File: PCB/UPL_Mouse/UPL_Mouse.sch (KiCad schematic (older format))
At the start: 10 parts, among them J1 PS2_5749180-1, J2 DB9_Female, J3 USB Micro_10118193-0001LF, J4 AVR-ISP-6, U1 MAX232DR, U2 ATTINY85-20SH

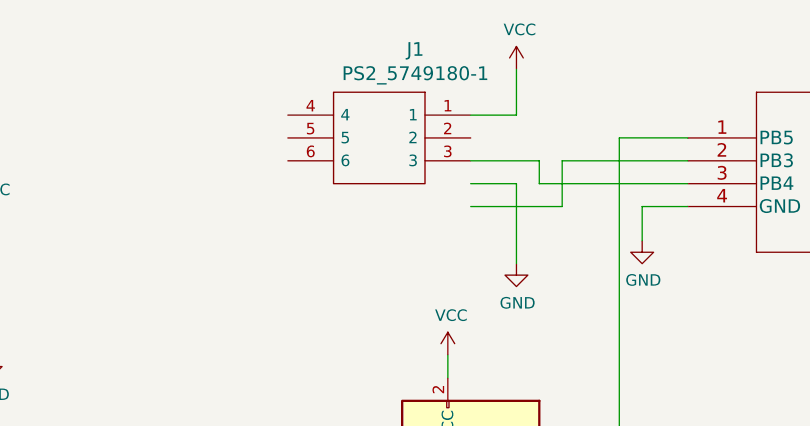
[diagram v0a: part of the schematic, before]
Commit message: Update Design and Code
Update in code regarding configuration of the chip.

Update in PCB due to wrong footprint mini din connector.
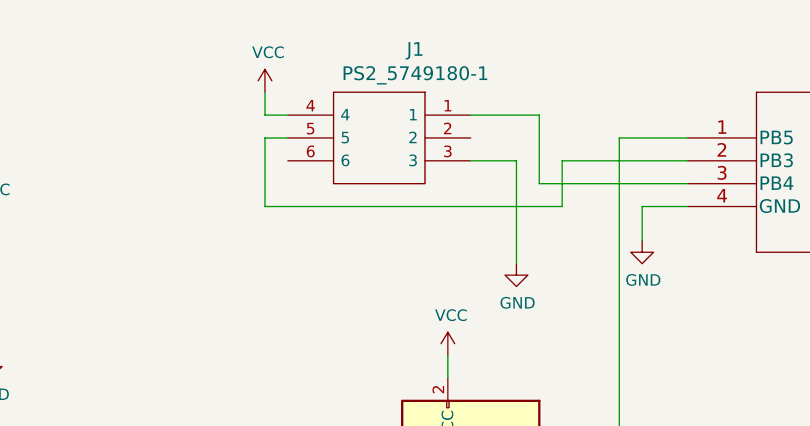
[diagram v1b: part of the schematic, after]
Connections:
- net GND: now also J1.3
- net VCC: now also J1.4; no longer J1.1
- net at U2.3 (PB4): now also J1.1; no longer J1.3
- net at J1.5: now also U2.2 (PB3)
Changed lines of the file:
@@
 	5250 2350 4600 2350
 Wire Wire Line
-	4600 2350 4600 2250
-Wire Wire Line
-	4600 2250 4300 2250
-Wire Wire Line
 	5250 2250 4700 2250
-Wire Wire Line
-	4700 2250 4700 2450
-Wire Wire Line
-	4700 2450 4300 2450
 Wire Wire Line
 	5050 2600 5050 2450
@@
 L power:VCC #PWR?
 U 1 1 6063A42F
-P 4500 1850
-F 0 "#PWR?" H 4500 1700 50  0001 C CNN
-F 1 "VCC" H 4515 2023 50  0000 C CNN
-F 2 "" H 4500 1850 50  0001 C CNN
-F 3 "" H 4500 1850 50  0001 C CNN
-	1    4500 1850
+P 3400 1950
+F 0 "#PWR?" H 3400 1800 50  0001 C CNN
+F 1 "VCC" H 3415 2123 50  0000 C CNN
+F 2 "" H 3400 1950 50  0001 C CNN
+F 3 "" H 3400 1950 50  0001 C CNN
+	1    3400 1950
 	1    0    0    -1
 $EndComp
-Wire Wire Line
-	4300 2350 4500 2350
-Wire Wire Line
-	4500 2350 4500 2700
-Wire Wire Line
-	4300 2050 4500 2050
-Wire Wire Line
-	4500 2050 4500 1850
 $Comp
 L power:VCC #PWR?
@@
 Wire Wire Line
 	2200 3050 2200 3100
+Wire Wire Line
+	3500 2050 3400 2050
+Wire Wire Line
+	3400 2050 3400 1950
+Wire Wire Line
+	4300 2250 4500 2250
+Wire Wire Line
+	4500 2250 4500 2700
+Wire Wire Line
+	3500 2150 3400 2150
+Wire Wire Line
+	3400 2150 3400 2450
+Wire Wire Line
+	3400 2450 4700 2450
+Wire Wire Line
+	4700 2450 4700 2250
+Wire Wire Line
+	4300 2050 4600 2050
+Wire Wire Line
+	4600 2050 4600 2350
 $EndSCHEMATC

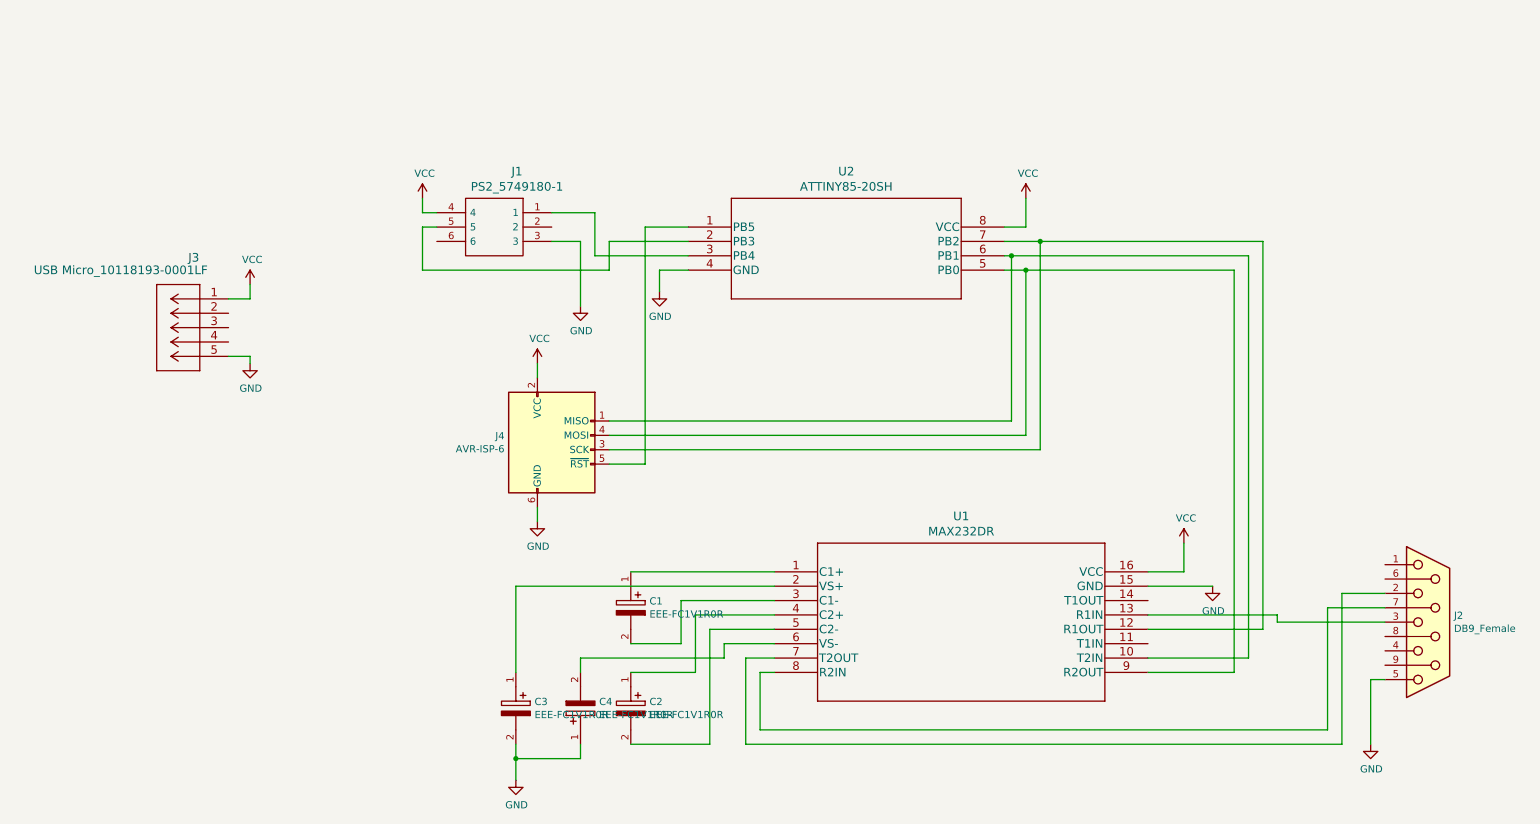
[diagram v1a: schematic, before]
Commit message: update with attiny84
update with attiny84 and rx tx
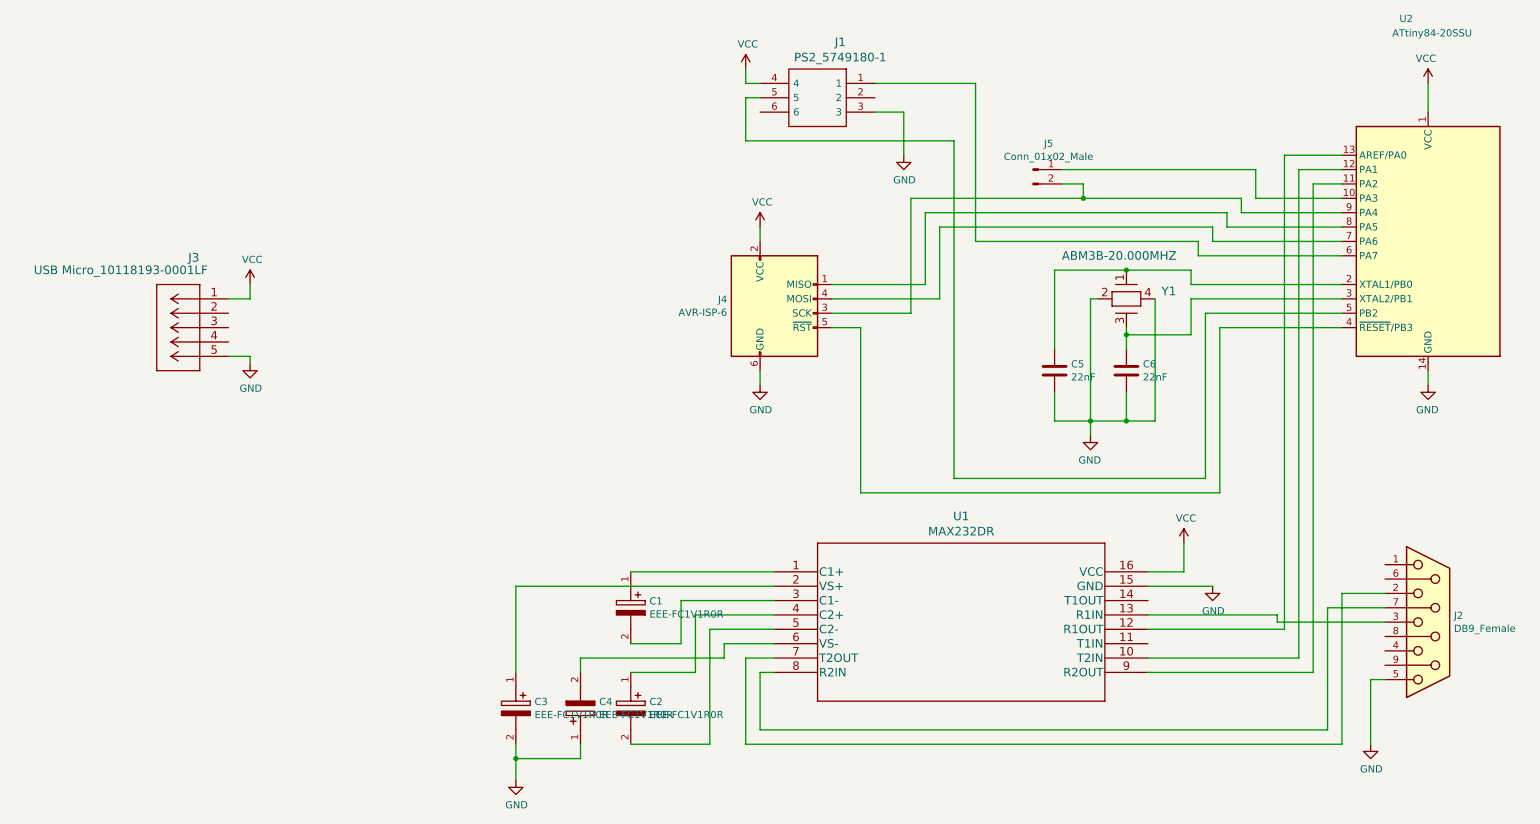
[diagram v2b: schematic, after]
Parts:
- removed U2: ATTINY85-20SH, BVKSound:ATTINY85-20SH, symbol BVKSound:ATTINY85-20SH
- added C5, C6: 22nF, Capacitor_SMD:C_0603_1608Metric, symbol Device:C
- added J5: Conn_01x02_Male, Connector_PinHeader_2.54mm:PinHeader_1x02_P2.54mm_Vertical, symbol Connector:Conn_01x02_Male
- added U2: ATtiny84-20SSU, Package_SO:SOIC-14_3.9x8.7mm_P1.27mm, symbol MCU_Microchip_ATtiny:ATtiny84-20SSU
- added Y1: ABM3B-20.000MHZ, BVKSound:ABM3B-20.000MHZ, symbol BVKSound:ABM3B-20.000MHZ
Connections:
- net GND: now also C5.2, C6.2, U2.14 (GND), Y1.2 (GND), Y1.4 (GND)
- net VCC: now also U2.1 (VCC)
- net at J1.1: now also U2.6 (PA7)
- net at J1.5: now also U2.5 (PB2)
- net at U1.10 (T2IN): now also U2.12 (PA1); no longer J4.1 (MISO)
- net at U1.12 (R1OUT): now also U2.13 (AREF/PA0); no longer J4.3 (SCK)
- net at U1.9 (R2OUT): now also U2.11 (PA2); no longer J4.4 (MOSI)
- net at J4.5 (~RST): now also U2.4 (~RESET~/PB3)
- new net: J4.1 (MISO), U2.8 (PA5)
- new net: J4.3 (SCK), J5.2 (Pin_2), U2.9 (PA4)
- new net: J4.4 (MOSI), U2.7 (PA6)
- new net: J5.1 (Pin_1), U2.10 (PA3)
- new net: C5.1, U2.2 (XTAL1/PB0), Y1.1
- new net: C6.1, U2.3 (XTAL2/PB1), Y1.3 (2)
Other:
- moved on the sheet: J1, J4
